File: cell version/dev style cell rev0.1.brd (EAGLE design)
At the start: 75 x 67 mm, 65 parts, among them CON1 SIMCARD_HOLDER_693022010811, SW1 BUTTON-TL3330AF130QG, U1 PIC24FJ128GB204, U3 24LC32A-SOT23-5, U4 TITAN-X1-GMS-3302, U5 AT45DB161E-SHD2B-T, U6 LSM6DSL, U7 PAM2305AAB330, U8 MCP73871, U9 SIM7000A, Y1 16MHz

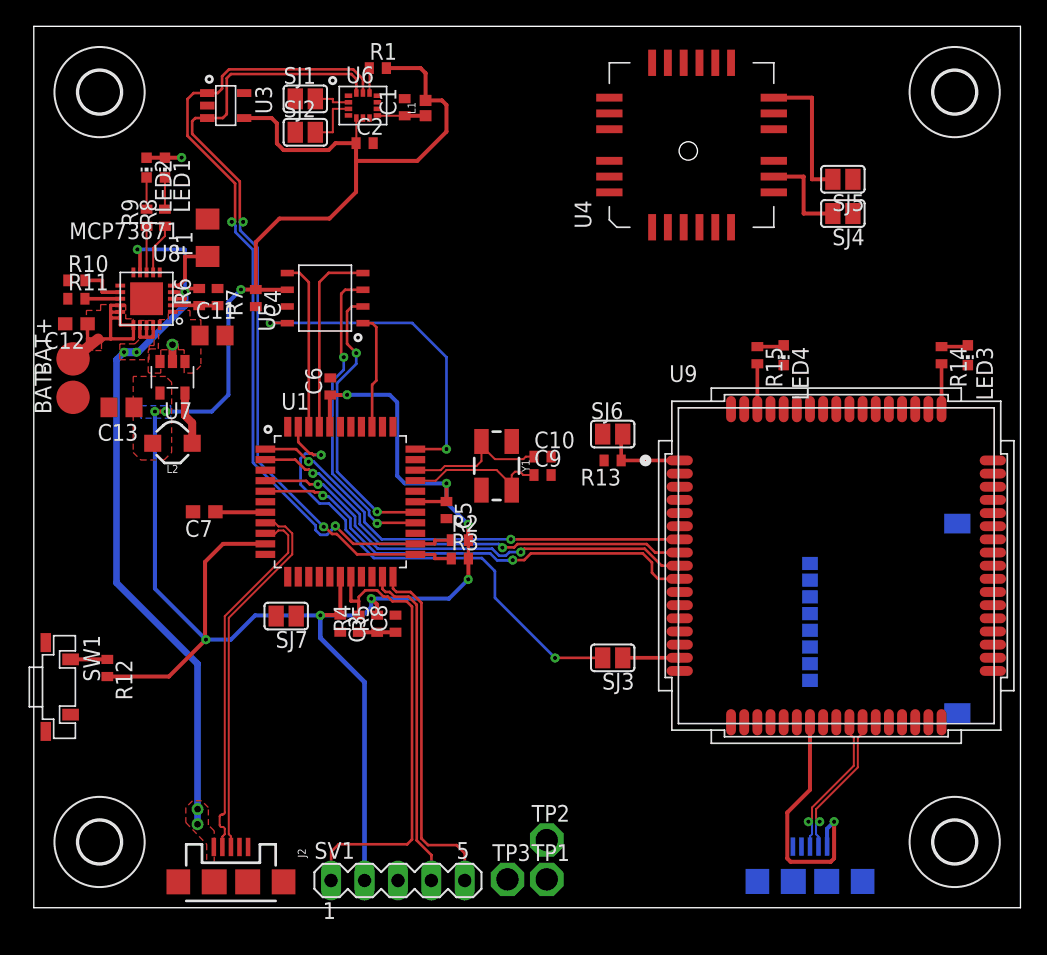
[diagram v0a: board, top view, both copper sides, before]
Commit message: added antennas and fiducials, finished routing, cleaned silk, added custom silk
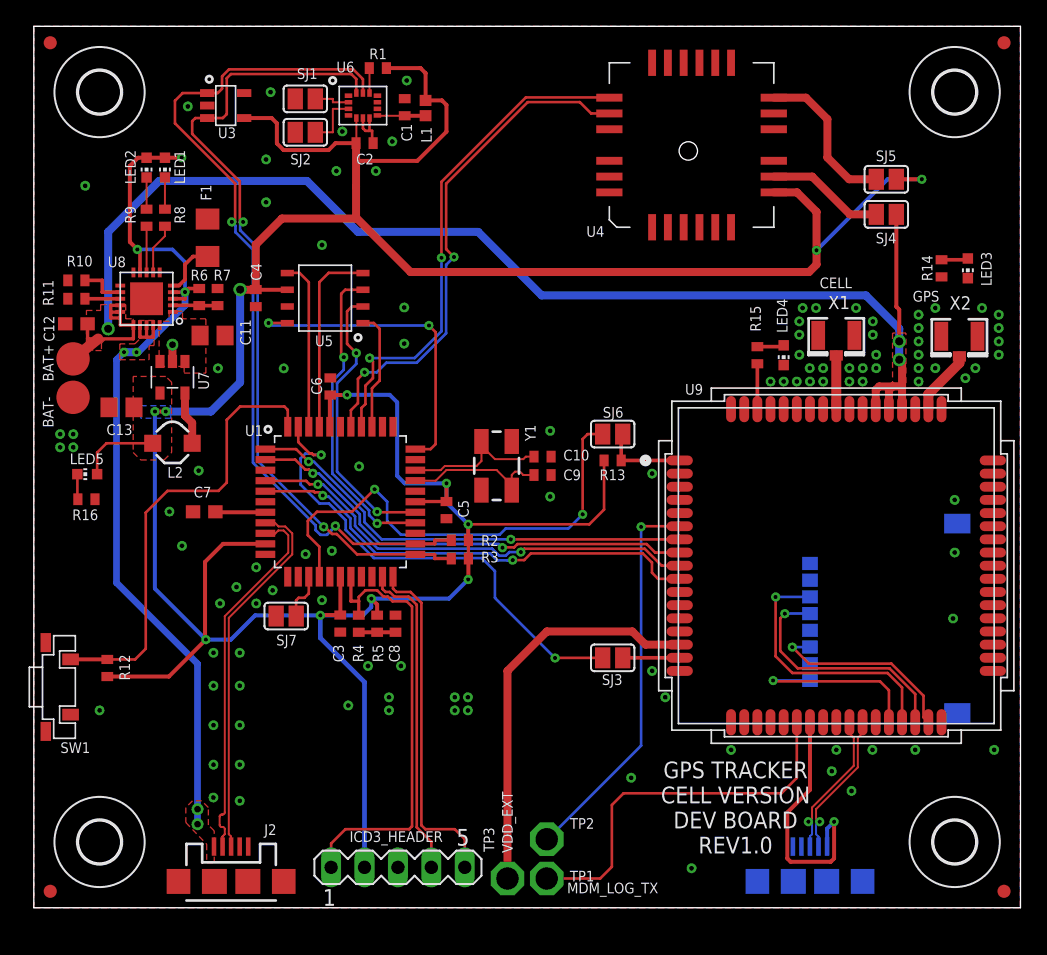
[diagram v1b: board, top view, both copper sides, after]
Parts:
- removed SV1: (no value), con-lstb:MA05-1
- added ICD3_HEADER: (no value), con-lstb:MA05-1
- added LED5: GREEN, adafruit:CHIP-LED0603
- added R16: 1K, resistor:R0402
- added U$1, U$2, U$3, U$4: FIDUCIAL, adafruit:FIDUCIAL_1MM
- added X1, X2: (no value), adafruit:U.FL
- moved LED3 6.60 mm to (71.0, 48.6)
- moved R14 6.60 mm to (69.0, 48.6)
- moved SJ4 3.30 mm to (64.8, 52.7)
- moved SJ5 3.30 mm to (64.8, 55.4)
- moved TP1 0.06 mm to (39.0, 2.22)
- moved TP3 0.06 mm to (36.0, 2.22)
- moved TP2 0.06 mm to (39.0, 5.21)
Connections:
- new net N$35: LED5.C, R16.2
- net 3.3V: now also ICD3_HEADER.2, LED5.A; no longer SV1.2
- net GND: now also ICD3_HEADER.3, R16.1, X1.1, X1.2, X2.1, X2.2; no longer SV1.3
- net MCLR: now also ICD3_HEADER.1; no longer SV1.1
- net N$21: now also X1.3
- net N$34: now also X2.3
- net PGC: now also ICD3_HEADER.5; no longer SV1.5
- net PGD: now also ICD3_HEADER.4; no longer SV1.4
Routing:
- net VBAT: track 15.4 -> 108.9 mm, vias 0 -> 3
- net 3.3V: track 181.3 -> 262.3 mm, vias 10 -> 12
- net RX0: track 0.00 -> 39.2 mm, vias 0 -> 2
- net TX0: track 0.00 -> 38.8 mm, vias 0 -> 2
- net BOOT0: track 0.00 -> 36.8 mm, vias 0 -> 2
- net BUTTON: track 2.79 -> 34.7 mm
- net N$36: track 0.00 -> 30.5 mm
- net N$32: track 0.00 -> 29.7 mm, vias 0 -> 1
- net N$29: track 0.00 -> 29.2 mm
- net N$26: track 0.00 -> 20.4 mm, vias 0 -> 1
- net N$25: track 0.00 -> 18.6 mm, vias 0 -> 1
- net N$27: track 0.00 -> 15.0 mm, vias 0 -> 1
- net N$23: track 0.00 -> 14.3 mm, vias 0 -> 1
- net V_USB: track 64.6 -> 72.1 mm
- net N$34: track 0.00 -> 4.99 mm
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- added copper zone on layer 1, net GND
- added copper zone on layer 16, net GND
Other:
- board text added: "BOOT_CFG"
- board text added: "CELL"
- board text added: "GPS"
- board text added: "GPS TRACKER CELL VERSION DEV BOARD REV1.0"
- board text added: "MDM_LOG_TX"
- board text added: "NETLIGHT"
- board text added: "STATUS"
- board text added: "VDD_EXT"
- board text added: "Veronica is the BEST!"

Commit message: pushed after a while
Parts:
- removed U9: SIM7000A, clackboard_lib:SIM7000A
- added U2: TELIT_LE866, clackboard_lib:TELIT_LE866
- moved J1 0.95 mm to (59.9, 1.62), flipped to the top
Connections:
- removed net IUR_IN: U1.3
- removed net IUR_OUT: U1.11
- removed net N$29: TP1.TP, U9.23
- removed net N$32: TP2.TP, U9.6
- removed net N$33: J1.VBUS, U9.24
- removed net N$34: U9.53, X2.3
- new net DIV_ANT: U2.C0
- new net MAIN_ANT: U2.G2, X2.3
- new net N$42: SJ3.1
- new net N$47: TP1.TP
- new net N$48: TP2.TP
- new net VBUS: J1.VBUS
- net GND: now also U2.A11, U2.A8, U2.B0, U2.C3, U2.D0, U2.D1, U2.D2, U2.E3, U2.F0, U2.F1, U2.F2, U2.F3, U2.F6, U2.G0, U2.G1, U2.G11, U2.G3, U2.G8; no longer U9.17, U9.18, U9.2, U9.29, U9.39, U9.45, U9.46, U9.54, U9.58, U9.59, U9.61, U9.62, U9.63, U9.64, U9.65
- net N$12: now also U2.E0, U2.E1, U2.E2; no longer SJ3.1, U9.16
- net N$18: no longer U9.52
- net N$21: no longer U9.60
- net N$22: no longer U9.1
- net N$23: now also U2.C7; no longer U9.30
- net N$25: now also CON1.C2, U2.B7; no longer CON1.C3, U9.32
- net N$26: now also CON1.C3, U2.A7; no longer CON1.C7, U9.31
- net N$27: now also CON1.C7, U2.A6; no longer CON1.C2, U9.33
- net N$31: no longer U9.66
- net N$36: no longer U9.15
- net PIC_CTS: now also U2.A1; no longer U9.8
- net PIC_RTS: now also U2.B1; no longer U9.7
- net PIC_RX: now also U2.C1; no longer U9.9
- net PIC_TX: now also U2.C2; no longer U9.10
- net SIM_N: now also U2.E6; no longer U9.28
- net SIM_P: now also U2.E5; no longer U9.27
- net VBAT: no longer U9.55, U9.56, U9.57
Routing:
- net N$32: track 29.7 -> 0.00 mm, vias 1 -> 0
- net N$29: track 29.2 -> 0.00 mm
- net SIM_P: track 11.5 -> 35.6 mm, vias 1 -> 0
- net SIM_N: track 11.5 -> 35.2 mm, vias 1 -> 0
- net N$33: track 19.7 -> 0.00 mm, vias 1 -> 0
- net PIC_RX: track 35.0 -> 47.0 mm
- net PIC_TX: track 35.6 -> 46.9 mm
- net N$26: track 20.4 -> 9.27 mm
- net PIC_RTS: track 34.8 -> 45.0 mm
- net PIC_CTS: track 35.1 -> 43.4 mm
- net N$25: track 18.6 -> 12.3 mm
- net N$27: track 15.0 -> 9.24 mm
- net N$23: track 14.3 -> 19.6 mm
- net N$34: track 4.99 -> 0.00 mm
- net VBAT: track 108.9 -> 104.3 mm
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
